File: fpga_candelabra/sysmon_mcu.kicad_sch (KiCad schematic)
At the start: 38 parts, among them J1 USB_C_Receptacle_USB2.0_14P, J2 DNP/MCU_DEBUG, SW1 TS-1187A, U17 W25Q128JVS, U21 PCA9306DC, U8 RP2040, Y1 12MHz 20pF

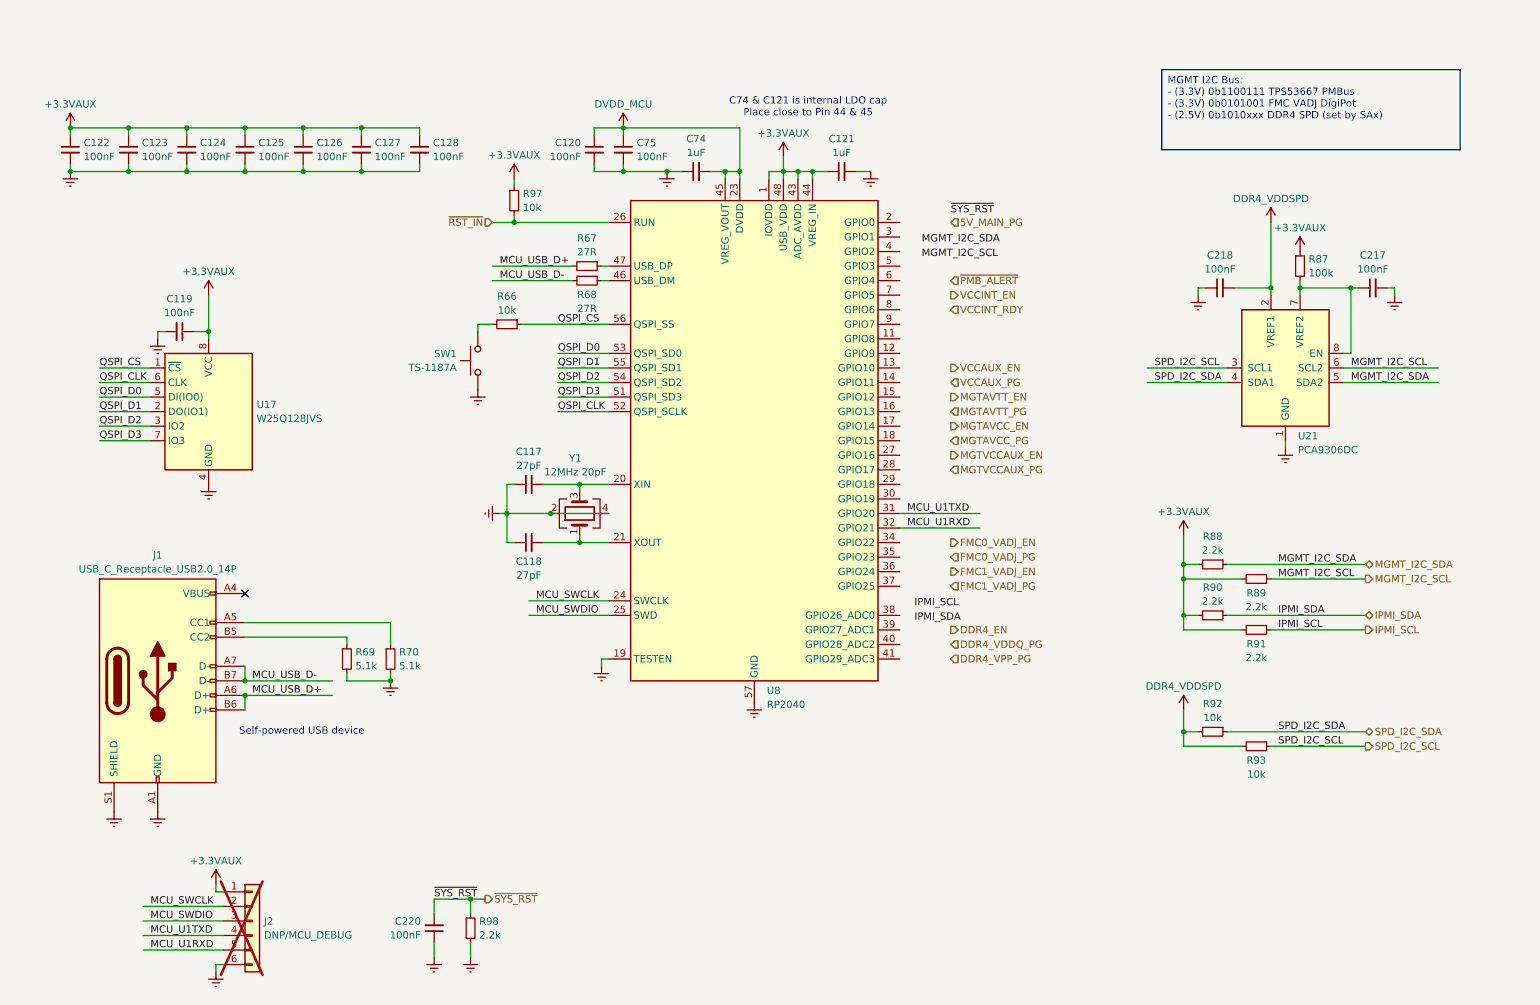
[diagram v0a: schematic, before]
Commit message: fpga_candelabra: add clock pll, refactor fmc power
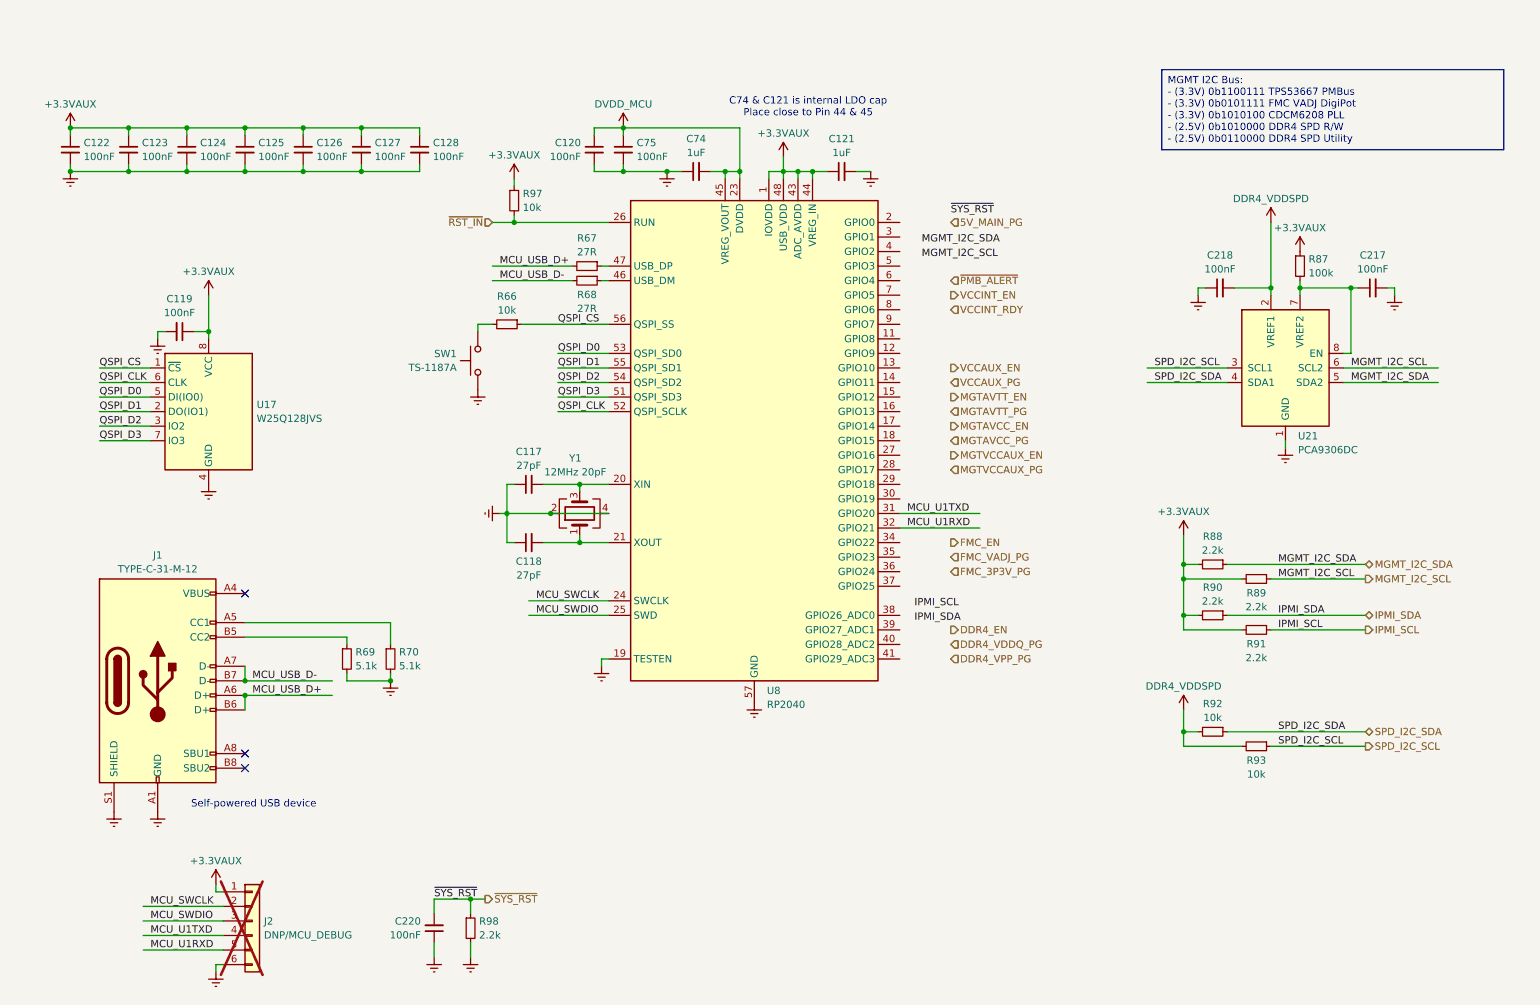
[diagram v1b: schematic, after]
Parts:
- J1: value USB_C_Receptacle_USB2.0_14P -> TYPE-C-31-M-12; symbol Connector:USB_C_Receptacle_USB2.0_14P -> Connector:USB_C_Receptacle_USB2.0_16P
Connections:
- no-connect marks 1 -> 3
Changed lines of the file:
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@@
 	)
 	(no_connect
+		(at 59.69 147.32)
+	)
+	(no_connect
 		(at 59.69 119.38)
 	)
+	(no_connect
+		(at 59.69 149.86)
+	)
 	(wire
 		(pts
@@
 		)
 	)
-	(text_box "MGMT I2C Bus:\n - (3.3V) 0b1100111 TPS53667 PMBus\n - (3.3V) 0b0101001 FMC VADJ DigiPot\n - (2.5V) 0b1010xxx DDR4 SPD (set by SAx)"
+	(text_box "MGMT I2C Bus:\n - (3.3V) 0b1100111 TPS53667 PMBus\n - (3.3V) 0b0101111 FMC VADJ DigiPot\n - (3.3V) 0b1010100 CDCM6208 PLL\n - (2.5V) 0b1010000 DDR4 SPD R/W\n - (2.5V) 0b0110000 DDR4 SPD Utility"
 		(exclude_from_sim no)
 		(at 219.71 27.94 0)
-		(size 52.07 13.97)
+		(size 59.69 13.97)
 		(stroke
 			(width 0)
@@
 	(text "Self-powered USB device"
 		(exclude_from_sim no)
-		(at 69.596 143.51 0)
+		(at 61.214 156.21 0)
 		(effects
 			(font
@@
 		)
 	)
-	(hierarchical_label "FMC0_VADJ_PG"
+	(hierarchical_label "FMC_VADJ_PG"
 		(shape input)
 		(at 182.88 113.03 0)
@@
 		)
 	)
-	(hierarchical_label "FMC0_VADJ_EN"
+	(hierarchical_label "FMC_EN"
 		(shape output)
 		(at 182.88 110.49 0)
@@
 		)
 	)
-	(hierarchical_label "FMC1_VADJ_EN"
-		(shape output)
+	(hierarchical_label "FMC_3P3V_PG"
+		(shape input)
 		(at 182.88 115.57 0)
 		(fields_autoplaced yes)
@@
 		)
 	)
-	(hierarchical_label "FMC1_VADJ_PG"
-		(shape input)
-		(at 182.88 118.11 0)
-		(fields_autoplaced yes)
-		(effects
-			(font
-				(size 1.27 1.27)
-			)
-			(justify left)
-		)
-	)
 	(symbol
 		(lib_id "Device:C_Small")
@@
 	)
 	(symbol
-		(lib_id "Connector:USB_C_Receptacle_USB2.0_14P")
+		(lib_id "Connector:USB_C_Receptacle_USB2.0_16P")
 		(at 44.45 134.62 0)
 		(unit 1)
@@
 			)
 		)
-		(property "Value" "USB_C_Receptacle_USB2.0_14P"
+		(property "Value" "TYPE-C-31-M-12"
 			(at 44.45 115.1198 0)
 			(effects
@@
 		(pin "A4"
 		)
+		(pin "A8"
+		)
+		(pin "B8"
+		)
 		(instances

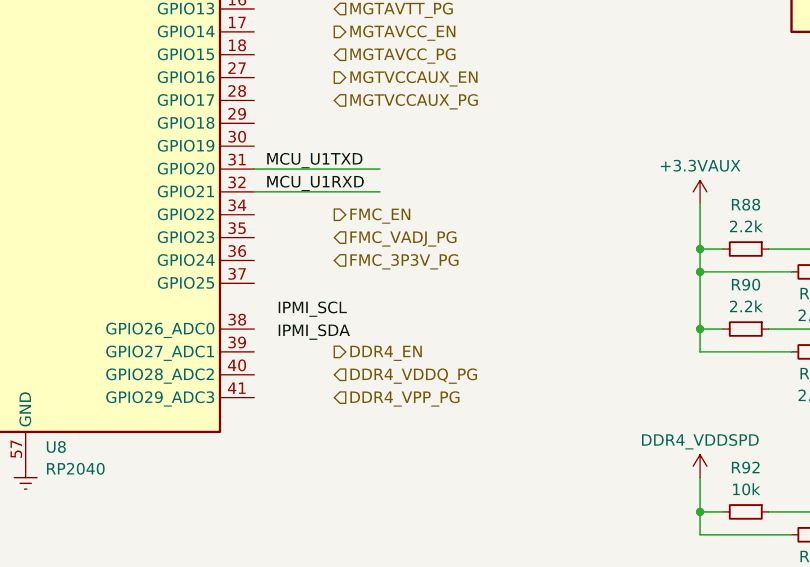
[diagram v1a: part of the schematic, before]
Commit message: candelabra: add i-pex extension ports, remove FMC1
* update bank/mgt allocation
* add basic pcb floorplanning

Signed-off-by: Yichuan Gao <gaoyichuan000@gmail.com>
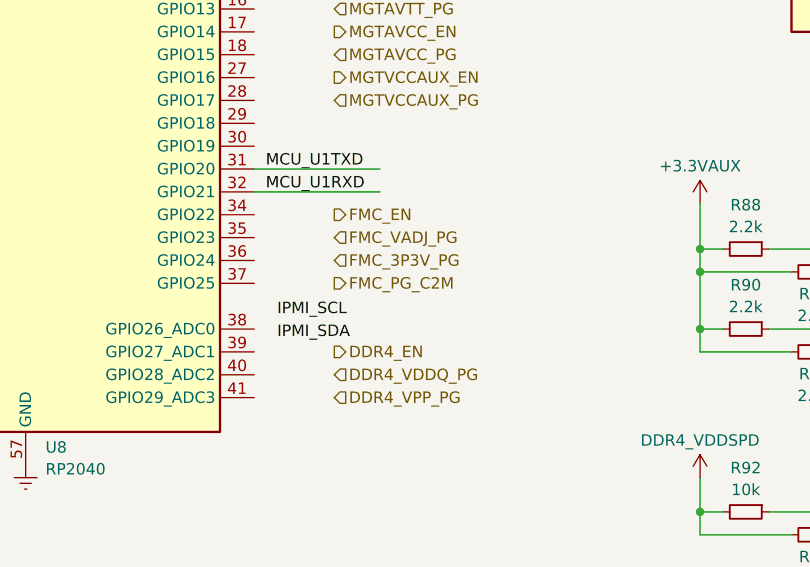
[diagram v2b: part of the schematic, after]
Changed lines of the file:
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@@
+		)
+	)
+	(hierarchical_label "FMC_PG_C2M"
+		(shape output)
+		(at 182.88 118.11 0)
+		(fields_autoplaced yes)
+		(effects
+			(font
+				(size 1.27 1.27)
+			)
+			(justify left)
 		)
 	)

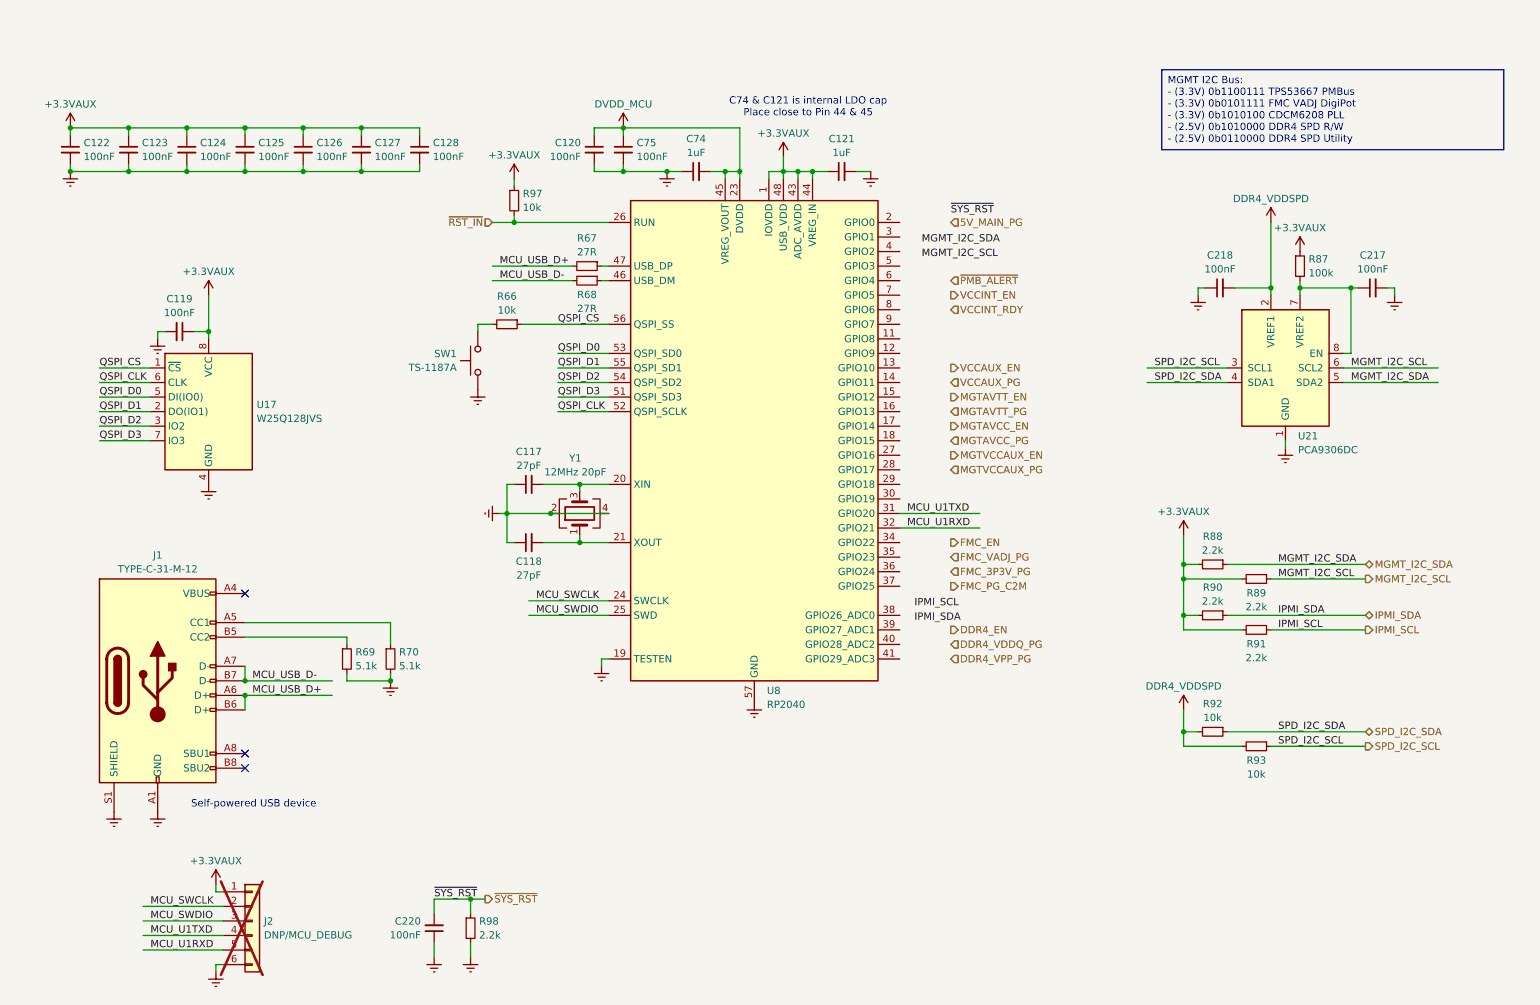
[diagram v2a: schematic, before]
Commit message: fpga_candelabra: major revision
* Finish DDR4 & QSFP+ & PCIe layout
* Change FMC to LPC
* Add mikroBUS extension
* 12V input & PDN updates
* FPGA config updates

Signed-off-by: Yichuan Gao <gaoyichuan000@gmail.com>
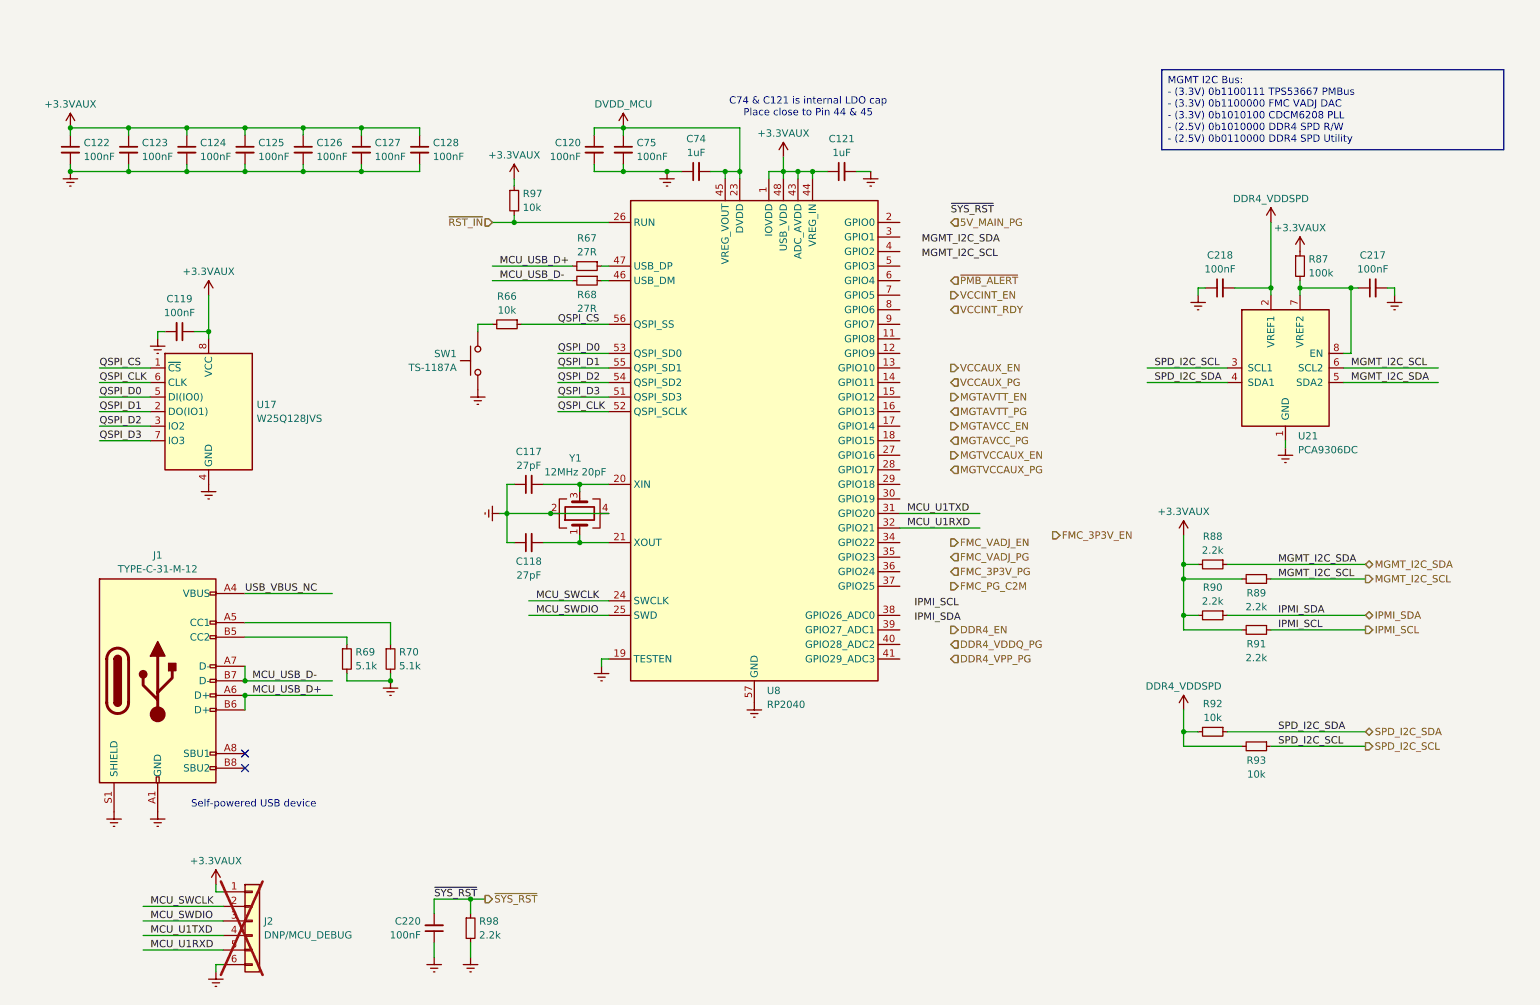
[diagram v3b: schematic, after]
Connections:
- net USB_VBUS_NC: now reaches J1.A4 (VBUS), J1.A9 (VBUS), J1.B4 (VBUS), J1.B9 (VBUS)
- no-connect marks 3 -> 2
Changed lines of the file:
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@@
-	)
-	(no_connect
-		(at 59.69 119.38)
 	)
 	(no_connect
@@
 	(wire
 		(pts
+			(xy 59.69 119.38) (xy 74.93 119.38)
+		)
+		(stroke
+			(width 0)
+			(type default)
+		)
+	)
+	(wire
+		(pts
 			(xy 59.69 137.16) (xy 74.93 137.16)
 		)
@@
 		)
 	)
-	(text_box "MGMT I2C Bus:\n - (3.3V) 0b1100111 TPS53667 PMBus\n - (3.3V) 0b0101111 FMC VADJ DigiPot\n - (3.3V) 0b1010100 CDCM6208 PLL\n - (2.5V) 0b1010000 DDR4 SPD R/W\n - (2.5V) 0b0110000 DDR4 SPD Utility"
+	(text_box "MGMT I2C Bus:\n - (3.3V) 0b1100111 TPS53667 PMBus\n - (3.3V) 0b1100000 FMC VADJ DAC\n - (3.3V) 0b1010100 CDCM6208 PLL\n - (2.5V) 0b1010000 DDR4 SPD R/W\n - (2.5V) 0b0110000 DDR4 SPD Utility"
 		(exclude_from_sim no)
 		(at 219.71 27.94 0)
@@
 		)
 	)
+	(label "USB_VBUS_NC"
+		(at 59.69 119.38 0)
+		(fields_autoplaced yes)
+		(effects
+			(font
+				(size 1.27 1.27)
+			)
+			(justify left bottom)
+		)
+	)
 	(label "MGMT_I2C_SDA"
 		(at 177.8 58.42 0)
@@
 		)
 	)
+	(hierarchical_label "FMC_3P3V_EN"
+		(shape output)
+		(at 200.66 109.22 0)
+		(fields_autoplaced yes)
+		(effects
+			(font
+				(size 1.27 1.27)
+			)
+			(justify left)
+		)
+	)
 	(hierarchical_label "MGTAVTT_PG"
 		(shape input)
@@
 		)
 	)
-	(hierarchical_label "FMC_EN"
+	(hierarchical_label "FMC_VADJ_EN"
 		(shape output)
 		(at 182.88 110.49 0)
